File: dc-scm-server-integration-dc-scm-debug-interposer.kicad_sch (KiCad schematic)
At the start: 8 parts

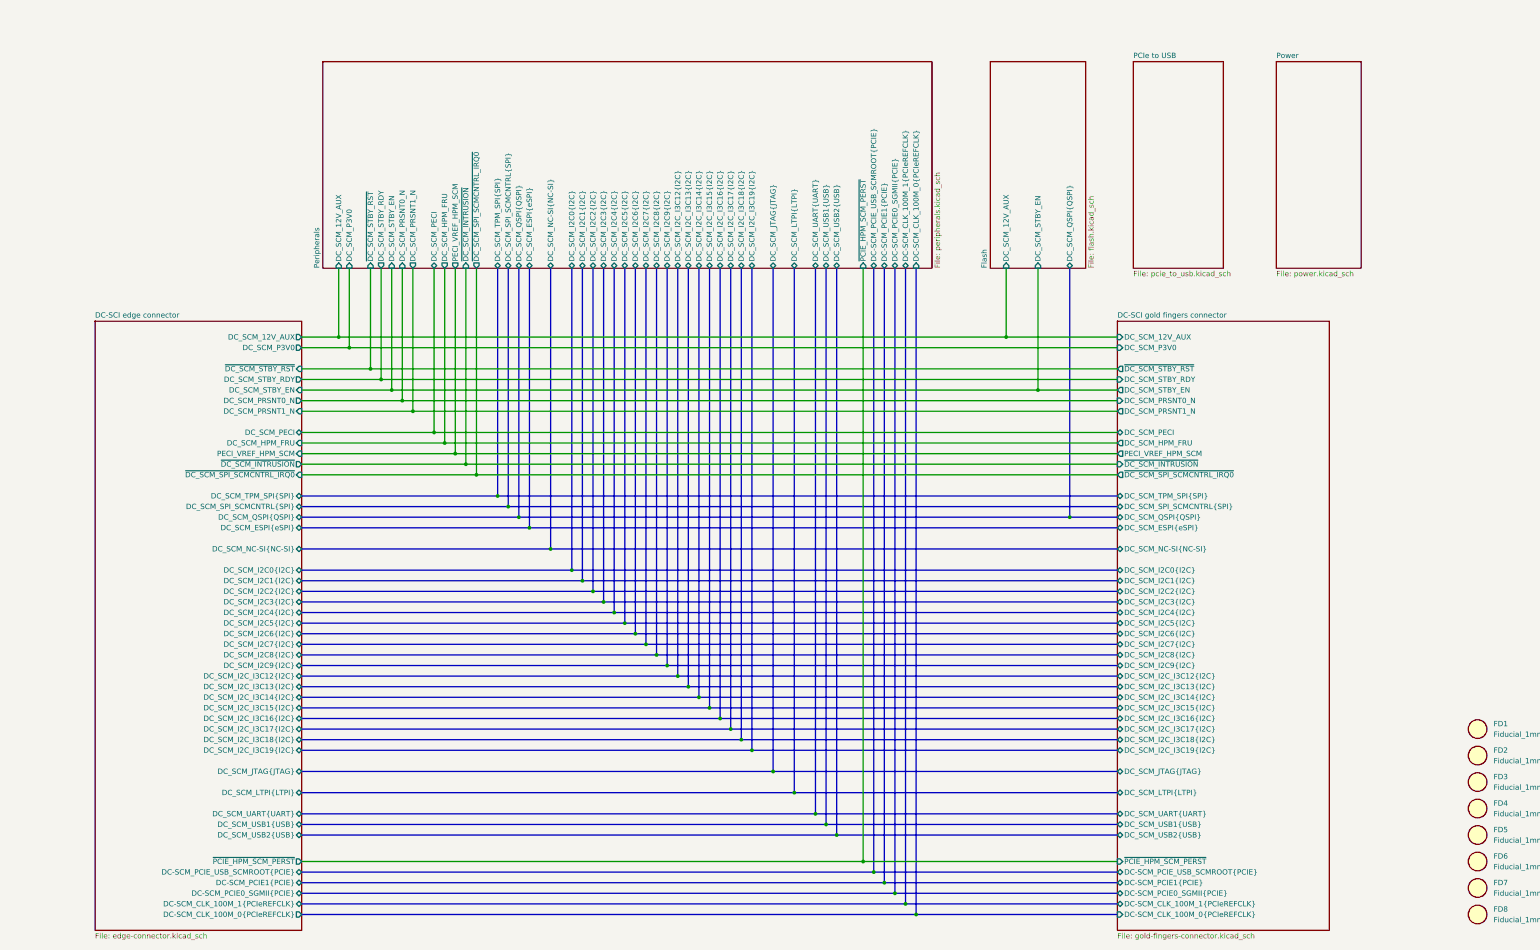
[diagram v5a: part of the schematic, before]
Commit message: [#100720] Finish schematic after PCIe to USB addition
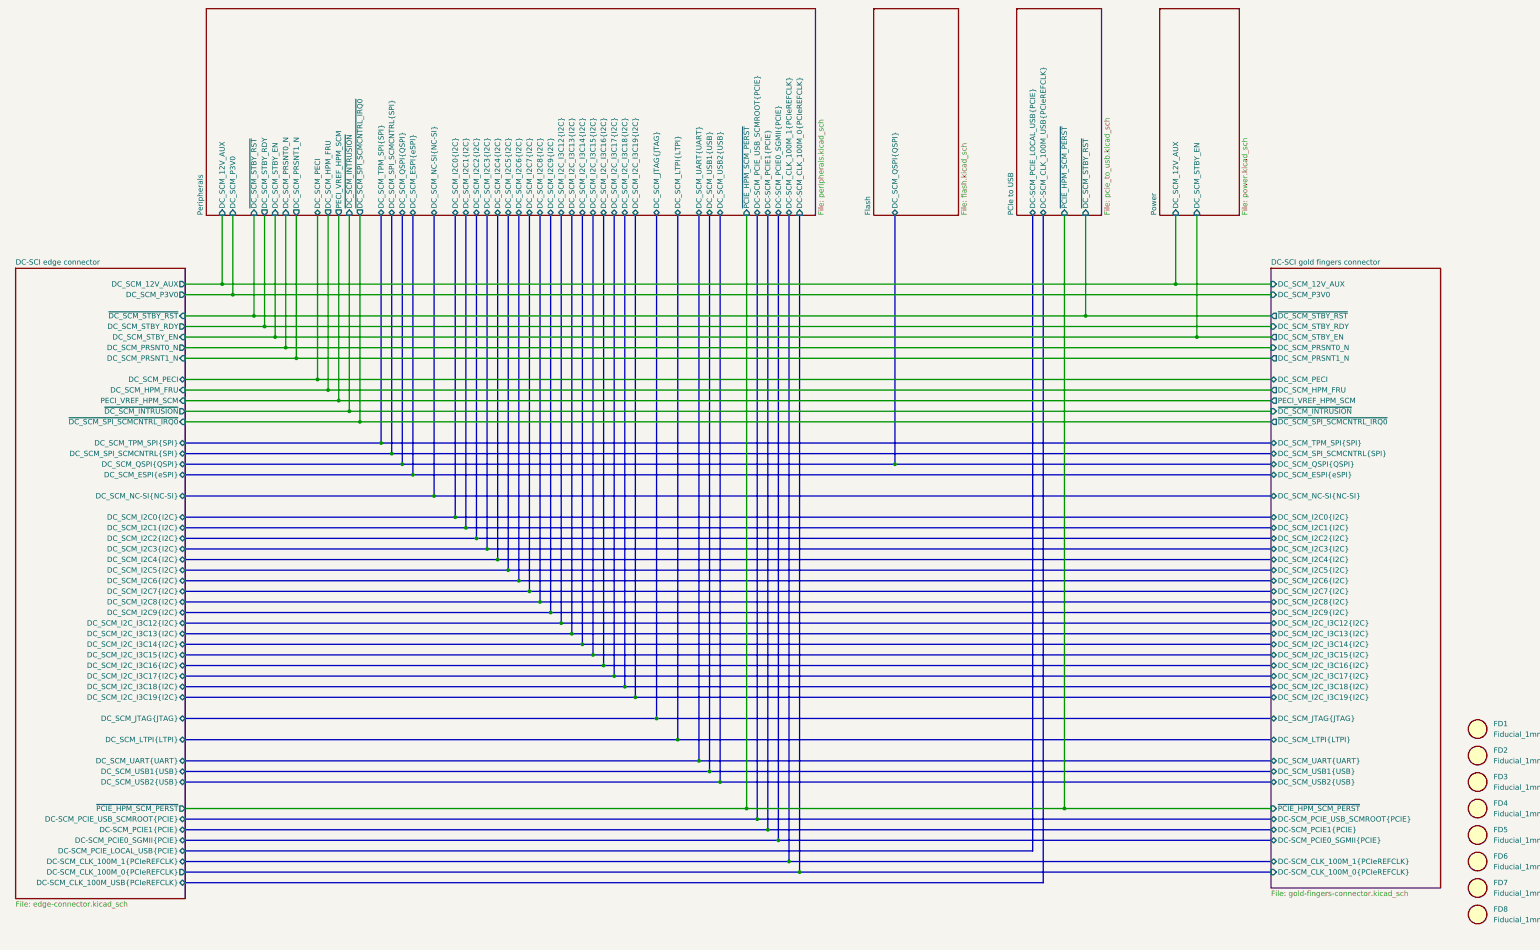
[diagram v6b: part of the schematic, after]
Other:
- sheet DC-SCI edge connector ports: added DC-SCM_CLK_100M_USB{PCIeREFCLK}, DC-SCM_PCIE_LOCAL_USB{PCIE}; removed none
- sheet Flash ports: added none; removed DC_SCM_12V_AUX, DC_SCM_STBY_EN
- sheet PCIe to USB ports: added DC-SCM_CLK_100M_USB{PCIeREFCLK}, DC-SCM_PCIE_LOCAL_USB{PCIE}, ~{DC_SCM_STBY_RST}, ~{PCIE_HPM_SCM_PERST}; removed none
- sheet Power ports: added DC_SCM_12V_AUX, DC_SCM_STBY_EN; removed none

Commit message: [#100720] Clear ERC
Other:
- sheet Peripherals ports: added none; removed DC-SCM_CLK_100M_0{PCIeREFCLK}, DC-SCM_CLK_100M_1{PCIeREFCLK}, DC-SCM_PCIE0_SGMII{PCIE}, DC-SCM_PCIE1{PCIE}, DC-SCM_PCIE_USB_SCMROOT{PCIE}, DC_SCM_LTPI{LTPI}, DC_SCM_USB1{USB}, DC_SCM_USB2{USB}, ~{PCIE_HPM_SCM_PERST}

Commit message: [#100720] Apply post review changes
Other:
- sheet DC-SCI edge connector ports: added none; removed DC-SCM_CLK_100M_USB{PCIeREFCLK}
- sheet DC-SCI gold fingers connector ports: added DC-SCM_PCIE_LOCAL_USB{PCIE}; removed none
- sheet PCIe to USB ports: added DC-SCM_CLK_100M_1{PCIeREFCLK}; removed DC-SCM_CLK_100M_USB{PCIeREFCLK}
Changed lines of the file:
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@@
 	)
 	(junction
-		(at 146.05 151.13)
+		(at 120.65 125.73)
 		(diameter 0)
 		(color 0 0 0 0)
 	)
 	(junction
-		(at 161.29 166.37)
+		(at 125.73 130.81)
 		(diameter 0)
 		(color 0 0 0 0)
@@
 	)
 	(junction
-		(at 100.33 105.41)
+		(at 130.81 135.89)
 		(diameter 0)
 		(color 0 0 0 0)
 	)
 	(junction
-		(at 176.53 181.61)
+		(at 179.07 184.15)
 		(diameter 0)
 		(color 0 0 0 0)
 	)
 	(junction
-		(at 153.67 158.75)
+		(at 158.75 163.83)
 		(diameter 0)
 		(color 0 0 0 0)
 	)
 	(junction
-		(at 125.73 130.81)
+		(at 171.45 176.53)
 		(diameter 0)
 		(color 0 0 0 0)
 	)
 	(junction
-		(at 171.45 176.53)
+		(at 176.53 181.61)
 		(diameter 0)
 		(color 0 0 0 0)
 	)
 	(junction
-		(at 166.37 171.45)
+		(at 143.51 148.59)
 		(diameter 0)
 		(color 0 0 0 0)
 	)
 	(junction
-		(at 168.91 173.99)
+		(at 95.25 100.33)
 		(diameter 0)
 		(color 0 0 0 0)
 	)
 	(junction
-		(at 118.11 123.19)
+		(at 161.29 166.37)
 		(diameter 0)
 		(color 0 0 0 0)
 	)
 	(junction
-		(at 130.81 135.89)
+		(at 100.33 105.41)
 		(diameter 0)
 		(color 0 0 0 0)
 	)
 	(junction
-		(at 87.63 92.71)
+		(at 118.11 123.19)
 		(diameter 0)
 		(color 0 0 0 0)
 	)
 	(junction
-		(at 191.77 196.85)
+		(at 184.15 189.23)
 		(diameter 0)
 		(color 0 0 0 0)
 	)
 	(junction
-		(at 151.13 156.21)
+		(at 260.35 218.44)
 		(diameter 0)
 		(color 0 0 0 0)
 	)
 	(junction
-		(at 184.15 189.23)
+		(at 219.71 135.89)
 		(diameter 0)
 		(color 0 0 0 0)
 	)
 	(junction
-		(at 90.17 95.25)
+		(at 115.57 120.65)
 		(diameter 0)
 		(color 0 0 0 0)
 	)
 	(junction
-		(at 156.21 161.29)
+		(at 173.99 179.07)
 		(diameter 0)
 		(color 0 0 0 0)
 	)
 	(junction
-		(at 133.35 138.43)
+		(at 102.87 107.95)
 		(diameter 0)
 		(color 0 0 0 0)
 	)
 	(junction
-		(at 219.71 135.89)
+		(at 196.85 207.01)
 		(diameter 0)
 		(color 0 0 0 0)
 	)
 	(junction
-		(at 110.49 115.57)
+		(at 146.05 151.13)
 		(diameter 0)
 		(color 0 0 0 0)
 	)
 	(junction
-		(at 181.61 186.69)
+		(at 186.69 191.77)
 		(diameter 0)
 		(color 0 0 0 0)
 	)
 	(junction
-		(at 260.35 218.44)
+		(at 153.67 158.75)
 		(diameter 0)
 		(color 0 0 0 0)
 	)
 	(junction
-		(at 148.59 153.67)
+		(at 255.27 231.14)
 		(diameter 0)
 		(color 0 0 0 0)
 	)
 	(junction
-		(at 113.03 118.11)
+		(at 191.77 196.85)
 		(diameter 0)
 		(color 0 0 0 0)
 	)
 	(junction
-		(at 95.25 100.33)
+		(at 151.13 156.21)
 		(diameter 0)
 		(color 0 0 0 0)
 	)
 	(junction
-		(at 163.83 168.91)
+		(at 110.49 115.57)
 		(diameter 0)
 		(color 0 0 0 0)
 	)
 	(junction
-		(at 158.75 163.83)
+		(at 156.21 161.29)
 		(diameter 0)
 		(color 0 0 0 0)
 	)
 	(junction
-		(at 128.27 133.35)
+		(at 105.41 110.49)
+		(diameter 0)
+		(color 0 0 0 0)
+	)
+	(junction
+		(at 148.59 153.67)
 		(diameter 0)
 		(color 0 0 0 0)
@@
 	)
 	(junction
-		(at 179.07 184.15)
+		(at 113.03 118.11)
 		(diameter 0)
 		(color 0 0 0 0)
 	)
 	(junction
-		(at 105.41 110.49)
+		(at 181.61 186.69)
 		(diameter 0)
 		(color 0 0 0 0)
 	)
 	(junction
-		(at 120.65 125.73)
+		(at 87.63 92.71)
 		(diameter 0)
 		(color 0 0 0 0)
 	)
 	(junction
-		(at 102.87 107.95)
+		(at 90.17 95.25)
 		(diameter 0)
 		(color 0 0 0 0)
 	)
 	(junction
-		(at 292.1 105.41)
+		(at 128.27 133.35)
 		(diameter 0)
 		(color 0 0 0 0)
 	)
 	(junction
-		(at 97.79 102.87)
+		(at 292.1 105.41)
 		(diameter 0)
 		(color 0 0 0 0)
 	)
 	(junction
-		(at 173.99 179.07)
+		(at 133.35 138.43)
 		(diameter 0)
 		(color 0 0 0 0)
@@
 	)
 	(junction
-		(at 196.85 207.01)
+		(at 166.37 171.45)
 		(diameter 0)
 		(color 0 0 0 0)
 	)
 	(junction
-		(at 115.57 120.65)
+		(at 252.73 228.6)
 		(diameter 0)
 		(color 0 0 0 0)
 	)
 	(junction
-		(at 143.51 148.59)
+		(at 163.83 168.91)
 		(diameter 0)
 		(color 0 0 0 0)
 	)
 	(junction
-		(at 186.69 191.77)
+		(at 97.79 102.87)
+		(diameter 0)
+		(color 0 0 0 0)
+	)
+	(junction
+		(at 168.91 173.99)
 		(diameter 0)
 		(color 0 0 0 0)
@@
 	(bus
 		(pts
+			(xy 255.27 231.14) (xy 307.34 231.14)
+		)
+		(stroke
+			(width 0)
+			(type default)
+		)
+	)
+	(bus
+		(pts
 			(xy 78.74 168.91) (xy 163.83 168.91)
 		)
@@
 	(bus
 		(pts
-			(xy 255.27 236.22) (xy 78.74 236.22)
-		)
-		(stroke
-			(width 0)
-			(type default)
-		)
-	)
-	(bus
-		(pts
 			(xy 163.83 76.2) (xy 163.83 168.91)
 		)
@@
 	(bus
 		(pts
-			(xy 78.74 228.6) (xy 252.73 228.6)
-		)
-		(stroke
-			(width 0)
-			(type default)
-		)
-	)
-	(bus
-		(pts
 			(xy 78.74 143.51) (xy 138.43 143.51)
 		)
@@
 	(bus
 		(pts
+			(xy 252.73 228.6) (xy 307.34 228.6)
+		)
+		(stroke
+			(width 0)
+			(type default)
+		)
+	)
+	(bus
+		(pts
 			(xy 158.75 163.83) (xy 307.34 163.83)
 		)
@@
 		)
 	)
+	(bus
+		(pts
+			(xy 78.74 228.6) (xy 252.73 228.6)
+		)
+		(stroke
+			(width 0)
+			(type default)
+		)
+	)
 	(wire
 		(pts
@@
 	(bus
 		(pts
-			(xy 78.74 231.14) (xy 307.34 231.14)
+			(xy 78.74 231.14) (xy 255.27 231.14)
 		)
 		(stroke
@@
 	(bus
 		(pts
-			(xy 255.27 76.2) (xy 255.27 236.22)
+			(xy 255.27 76.2) (xy 255.27 231.14)
 		)
 		(stroke
@@
 			)
 		)
+		(pin "DC-SCM_PCIE_LOCAL_USB{PCIE}" bidirectional
+			(at 307.34 228.6 180)
+			(effects
+				(font
+					(size 1.27 1.27)
+				)
+				(justify left)
+			)
+		)
 		(instances
 			(project "dc-scm-server-integration-dc-scm-debug-interposer"
@@
 	(sheet
 		(at 38.1 88.9)
-		(size 40.64 151.13)
+		(size 40.64 148.59)
 		(exclude_from_sim no)
 		(in_bom yes)
@@
 		)
 		(property "Sheetfile" "edge-connector.kicad_sch"
-			(at 38.1 240.6146 0)
+			(at 38.1 238.0746 0)
 			(show_name no)
 			(do_not_autoplace no)
@@
 			)
 		)
-		(pin "DC-SCM_CLK_100M_USB{PCIeREFCLK}" bidirectional
-			(at 78.74 236.22 0)
-			(effects
-				(font
-					(size 1.27 1.27)
-				)
-				(justify right)
-			)
-		)
 		(pin "DC-SCM_PCIE_LOCAL_USB{PCIE}" bidirectional
 			(at 78.74 228.6 0)
@@
 			)
 		)
-		(pin "DC-SCM_CLK_100M_USB{PCIeREFCLK}" bidirectional
-			(at 255.27 76.2 270)
+		(pin "DC-SCM_PCIE_LOCAL_USB{PCIE}" bidirectional
+			(at 252.73 76.2 270)
 			(effects
 				(font
@@
 			)
 		)
-		(pin "DC-SCM_PCIE_LOCAL_USB{PCIE}" bidirectional
-			(at 252.73 76.2 270)
+		(pin "~{DC_SCM_STBY_RST}" input
+			(at 265.43 76.2 270)
 			(effects
 				(font
@@
 			)
 		)
-		(pin "~{DC_SCM_STBY_RST}" input
-			(at 265.43 76.2 270)
+		(pin "~{PCIE_HPM_SCM_PERST}" input
+			(at 260.35 76.2 270)
 			(effects
 				(font
@@
 			)
 		)
-		(pin "~{PCIE_HPM_SCM_PERST}" input
-			(at 260.35 76.2 270)
+		(pin "DC-SCM_CLK_100M_1{PCIeREFCLK}" bidirectional
+			(at 255.27 76.2 270)
 			(effects
 				(font
